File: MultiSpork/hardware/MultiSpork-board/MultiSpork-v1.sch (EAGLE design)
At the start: 215 parts, among them J1 U.FL, Q2 32.768 kHz, Q3 40 MHz, Q4 MMBT3904, Q5 MMBT3904, U1 USD-SOCKETNEW, U10 M25PX80, U2 SAM3SA-MU, U3 MAX11300GTL, U4 LT3580EMS8E, U5 LT3580EMS8E, U6 LT3580EMS8E, U7 MCP73831, U8 LT3580EMS8E, U9 CC3100

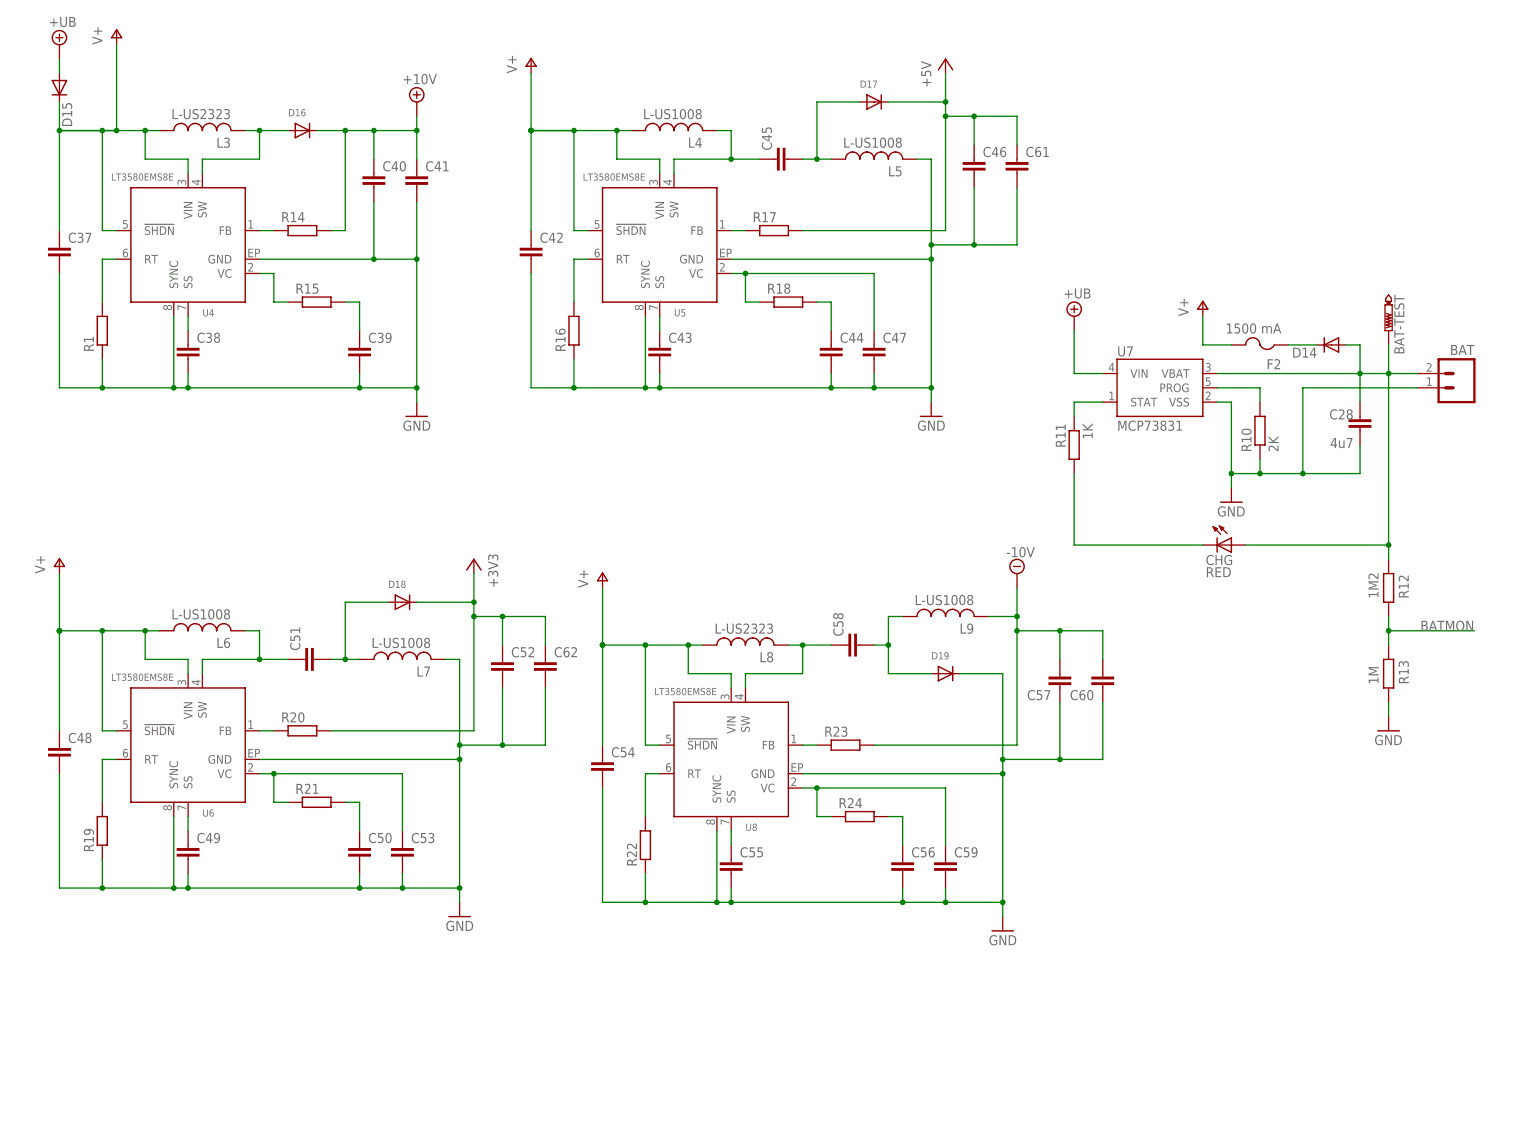
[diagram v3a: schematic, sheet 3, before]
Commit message: -- Updated MAX11300 footprint with rounded pads to account for minimum clearances at the corners -- Added a switch to turn the regulators on and off -- Routed USB -- Routed SPI busses -- Routed analog inputs to protection components
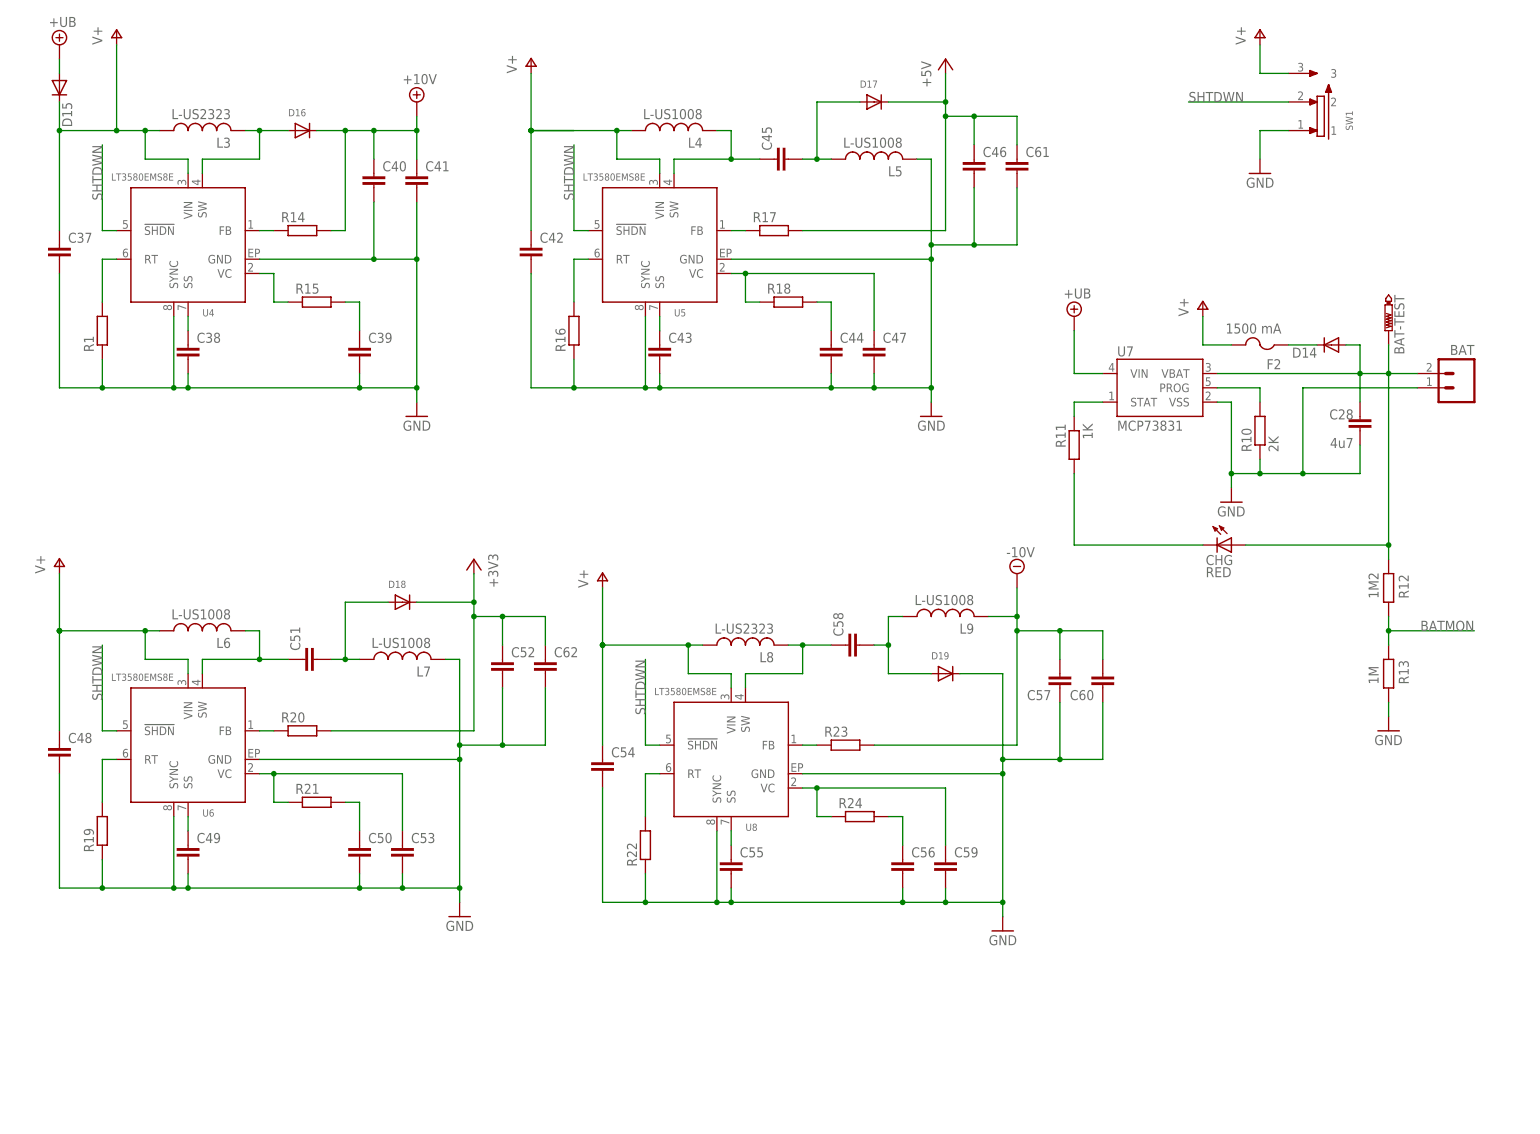
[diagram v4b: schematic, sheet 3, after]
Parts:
- added SW1: JS102011SAQN, logos-switch:JS102011SAQN
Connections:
- new net SHTDWN: SW1.2, U4.!SHDN!, U5.!SHDN!, U6.!SHDN!, U8.!SHDN!
- net GND: now also SW1.1
- net V+: now also SW1.3; no longer U4.!SHDN!, U5.!SHDN!, U6.!SHDN!, U8.!SHDN!
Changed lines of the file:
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@@
 <part name="R40" library="resistor" deviceset="R-EU_" device="R1206"/>
 <part name="J1" library="SparkFun-Connectors" deviceset="U.FL" device="" value="U.FL"/>
+<part name="SW1" library="logos-switch" deviceset="JS102011SAQN" device=""/>
+<part name="P+7" library="supply1" deviceset="V+" device=""/>
+<part name="GND29" library="supply1" deviceset="GND" device=""/>
 </parts>
 <sheets>
@@
 <instance part="C52" gate="G$1" x="93.98" y="88.9"/>
 <instance part="C62" gate="G$1" x="101.6" y="88.9"/>
+<instance part="SW1" gate="G$1" x="238.76" y="187.96" rot="MR90"/>
+<instance part="P+7" gate="1" x="228.6" y="200.66"/>
+<instance part="GND29" gate="1" x="228.6" y="175.26" rot="MR0"/>
 </instances>
 <busses>
@@
 <junction x="193.04" y="71.12"/>
 </segment>
+<segment>
+<pinref part="SW1" gate="G$1" pin="1"/>
+<pinref part="GND29" gate="1" pin="GND"/>
+<wire x1="228.6" y1="177.8" x2="228.6" y2="182.88" width="0.1524" layer="91"/>
+<wire x1="228.6" y1="182.88" x2="233.68" y2="182.88" width="0.1524" layer="91"/>
+</segment>
 </net>
 <net name="+3V3" class="0">
@@
 <segment>
 <pinref part="P+5" gate="1" pin="V+"/>
-<wire x1="15.24" y1="182.88" x2="25.4" y2="182.88" width="0.1524" layer="91"/>
 <wire x1="25.4" y1="182.88" x2="25.4" y2="198.12" width="0.1524" layer="91"/>
 <pinref part="D15" gate="G$1" pin="C"/>
@@
 <wire x1="30.48" y1="182.88" x2="33.02" y2="182.88" width="0.1524" layer="91"/>
 <wire x1="30.48" y1="182.88" x2="25.4" y2="182.88" width="0.1524" layer="91"/>
-<wire x1="25.4" y1="182.88" x2="22.86" y2="182.88" width="0.1524" layer="91"/>
-<wire x1="22.86" y1="182.88" x2="22.86" y2="165.1" width="0.1524" layer="91"/>
-<pinref part="U4" gate="G$1" pin="!SHDN!"/>
-<wire x1="22.86" y1="165.1" x2="25.4" y2="165.1" width="0.1524" layer="91"/>
 <junction x="30.48" y="182.88"/>
 <pinref part="C37" gate="G$1" pin="1"/>
-<wire x1="22.86" y1="182.88" x2="15.24" y2="182.88" width="0.1524" layer="91"/>
+<wire x1="25.4" y1="182.88" x2="15.24" y2="182.88" width="0.1524" layer="91"/>
 <wire x1="15.24" y1="182.88" x2="15.24" y2="165.1" width="0.1524" layer="91"/>
-<junction x="22.86" y="182.88"/>
 <junction x="25.4" y="182.88"/>
 <junction x="15.24" y="182.88"/>
@@
 <wire x1="114.3" y1="182.88" x2="116.84" y2="182.88" width="0.1524" layer="91"/>
 <wire x1="114.3" y1="182.88" x2="99.06" y2="182.88" width="0.1524" layer="91"/>
-<wire x1="106.68" y1="182.88" x2="106.68" y2="165.1" width="0.1524" layer="91"/>
-<pinref part="U5" gate="G$1" pin="!SHDN!"/>
-<wire x1="106.68" y1="165.1" x2="109.22" y2="165.1" width="0.1524" layer="91"/>
 <junction x="114.3" y="182.88"/>
 <pinref part="C42" gate="G$1" pin="1"/>
 <wire x1="106.68" y1="182.88" x2="99.06" y2="182.88" width="0.1524" layer="91"/>
 <wire x1="99.06" y1="182.88" x2="99.06" y2="165.1" width="0.1524" layer="91"/>
-<junction x="106.68" y="182.88"/>
 <junction x="99.06" y="182.88"/>
 <junction x="99.06" y="182.88"/>
@@
 <pinref part="L6" gate="G$1" pin="1"/>
 <wire x1="30.48" y1="93.98" x2="33.02" y2="93.98" width="0.1524" layer="91"/>
-<wire x1="30.48" y1="93.98" x2="22.86" y2="93.98" width="0.1524" layer="91"/>
-<wire x1="22.86" y1="93.98" x2="22.86" y2="76.2" width="0.1524" layer="91"/>
-<pinref part="U6" gate="G$1" pin="!SHDN!"/>
-<wire x1="22.86" y1="76.2" x2="25.4" y2="76.2" width="0.1524" layer="91"/>
 <junction x="30.48" y="93.98"/>
 <pinref part="C48" gate="G$1" pin="1"/>
-<wire x1="22.86" y1="93.98" x2="15.24" y2="93.98" width="0.1524" layer="91"/>
+<wire x1="30.48" y1="93.98" x2="15.24" y2="93.98" width="0.1524" layer="91"/>
 <wire x1="15.24" y1="93.98" x2="15.24" y2="76.2" width="0.1524" layer="91"/>
-<junction x="22.86" y="93.98"/>
 <junction x="15.24" y="93.98"/>
 <junction x="15.24" y="93.98"/>
@@
 <pinref part="L8" gate="G$1" pin="1"/>
 <wire x1="127" y1="91.44" x2="129.54" y2="91.44" width="0.1524" layer="91"/>
-<wire x1="127" y1="91.44" x2="119.38" y2="91.44" width="0.1524" layer="91"/>
-<wire x1="119.38" y1="91.44" x2="119.38" y2="73.66" width="0.1524" layer="91"/>
-<pinref part="U8" gate="G$1" pin="!SHDN!"/>
-<wire x1="119.38" y1="73.66" x2="121.92" y2="73.66" width="0.1524" layer="91"/>
 <junction x="127" y="91.44"/>
 <pinref part="C54" gate="G$1" pin="1"/>
-<wire x1="119.38" y1="91.44" x2="111.76" y2="91.44" width="0.1524" layer="91"/>
+<wire x1="127" y1="91.44" x2="111.76" y2="91.44" width="0.1524" layer="91"/>
 <wire x1="111.76" y1="91.44" x2="111.76" y2="73.66" width="0.1524" layer="91"/>
-<junction x="119.38" y="91.44"/>
 <junction x="111.76" y="91.44"/>
 <junction x="111.76" y="91.44"/>
+</segment>
+<segment>
+<pinref part="SW1" gate="G$1" pin="3"/>
+<pinref part="P+7" gate="1" pin="V+"/>
+<wire x1="228.6" y1="198.12" x2="228.6" y2="193.04" width="0.1524" layer="91"/>
+<wire x1="228.6" y1="193.04" x2="233.68" y2="193.04" width="0.1524" layer="91"/>
 </segment>
 </net>
@@
 </segment>
 </net>
+<net name="SHTDWN" class="0">
+<segment>
+<pinref part="SW1" gate="G$1" pin="2"/>
+<wire x1="233.68" y1="187.96" x2="215.9" y2="187.96" width="0.1524" layer="91"/>
+<label x="215.9" y="187.96" size="1.778" layer="95"/>
+</segment>
+<segment>
+<pinref part="U8" gate="G$1" pin="!SHDN!"/>
+<wire x1="119.38" y1="73.66" x2="121.92" y2="73.66" width="0.1524" layer="91"/>
+<wire x1="119.38" y1="73.66" x2="119.38" y2="88.9" width="0.1524" layer="91"/>
+<label x="119.38" y="88.9" size="1.778" layer="95" rot="MR270"/>
+</segment>
+<segment>
+<pinref part="U6" gate="G$1" pin="!SHDN!"/>
+<wire x1="22.86" y1="76.2" x2="25.4" y2="76.2" width="0.1524" layer="91"/>
+<wire x1="22.86" y1="76.2" x2="22.86" y2="91.44" width="0.1524" layer="91"/>
+<label x="22.86" y="91.44" size="1.778" layer="95" rot="MR270"/>
+</segment>
+<segment>
+<pinref part="U4" gate="G$1" pin="!SHDN!"/>
+<wire x1="22.86" y1="165.1" x2="25.4" y2="165.1" width="0.1524" layer="91"/>
+<wire x1="22.86" y1="165.1" x2="22.86" y2="180.34" width="0.1524" layer="91"/>
+<label x="22.86" y="180.34" size="1.778" layer="95" rot="MR270"/>
+</segment>
+<segment>
+<pinref part="U5" gate="G$1" pin="!SHDN!"/>
+<wire x1="106.68" y1="165.1" x2="109.22" y2="165.1" width="0.1524" layer="91"/>
+<wire x1="106.68" y1="165.1" x2="106.68" y2="180.34" width="0.1524" layer="91"/>
+<label x="106.68" y="180.34" size="1.778" layer="95" rot="MR270"/>
+</segment>
+</net>

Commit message: Finished routing
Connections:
- net N$115 renamed D1P
- net N$116 renamed D1N
- net N$117 renamed D0N
- net N$118 renamed D0P
- net N$19 renamed PLL-GND
- net N$32 renamed ADC_REF
- net N$33 renamed DAC_REF
- net N$34 renamed PORT00'
- net N$35 renamed PORT01'
- net N$36 renamed PORT02'
- net N$37 renamed PORT03'
- net N$38 renamed PORT04'
- net N$39 renamed PORT05'
- net N$40 renamed PORT06'
- net N$41 renamed PORT07'
- net N$42 renamed PORT08'
- net N$43 renamed PORT09'
- net N$44 renamed PORT10'
- net N$45 renamed PORT11'
- net N$46 renamed PORT12'
- net N$47 renamed PORT13'
- net N$49 renamed PORT14'
- net N$50 renamed PORT15'
- net N$51 renamed PORT16'
- net N$52 renamed PORT17'
- net N$53 renamed PORT18'
- net N$54 renamed PORT19'
- net N$56 renamed VDD_IO
- net N$79 renamed VIN_IO2
- net N$80 renamed VIN_DIG
- net N$81 renamed VIN_ANA
- net N$83 renamed VIN_PA
- net N$84 renamed ANA_SW
- net N$85 renamed VDD_PA
- net N$87 renamed PA_SWP
- net N$88 renamed PA_SWN
- net N$90 renamed VDD_DIG
- net N$92 renamed VDD_RAM
- net N$93 renamed VDD_PLL
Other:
- moved on the sheet: C24, L12, U3-REF

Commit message: .\s5uqt2as.xa0.txt
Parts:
- ACC, JP2, JP3: PARTNO (none) -> *
- ANALOG: PARTNO (none) -> 76385-316LF
- C1, C2, C3, C4, C5: PARTNO (none) -> VJ0603A330JXACW1BC
- C10, C12, C13, C14, C15, C19, C20, C22, C25, C26, C29, C31, C33, C63, C67, C69, C70, C71, C73, C74, C75, C76, C77, C80, C85, C9: PARTNO (none) -> CC0603KRX7R9BB104
- C11, C30, C32, C34: PARTNO (none) -> UMK107BJ105KA-T
- C16, C17, C21, C24, C27, C64, C65, C66: PARTNO (none) -> GRM188F51A475ZE20D
- C18, C68, C72: PARTNO (none) -> EMK107BBJ106MA-T
- C23: PARTNO (none) -> C1608X7R1A225K
- C35, C36, C81, C82: value (none) -> 33p; PARTNO (none) -> VJ0603A330JXACW1BC
- C37, C42, C48, C54: value (none) -> 4u7; PARTNO (none) -> TMK325B7475KN-T
- C38, C43, C49, C55: value (none) -> 100n; PARTNO (none) -> CC0603KRX7R9BB104
- C39, C56: value (none) -> 2n2; PARTNO (none) -> VJ0603Y222KXACW1BC
- C40, C41, C46, C52, C57, C60, C61, C62: value (none) -> 10u; PARTNO (none) -> UMK325BJ106MM
- C44, C50: value (none) -> 1n; PARTNO (none) -> UMK107SD102KA-T
- C45, C51, C58: value (none) -> 1u; PARTNO (none) -> TMK325B7105KD-T
- C47, C53: value (none) -> 22p; PARTNO (none) -> GQM1885C1H220JB01D
- C59: value (none) -> DNP; DNP (none) -> T; PARTNO (none) -> DNP
- C6: PARTNO (none) -> CL10B103KB8NCNC
- C7, C8: PARTNO (none) -> C3216X5R1E106M
- C78, C79: PARTNO (none) -> GRM31CR61C226ME15L
- C83, C84: value (none) -> 15p; PARTNO (none) -> VJ0603A150JXACW1BC
- C86, C87: PARTNO (none) -> TAJC107K016RNJ
- D1, D10, D11, D12, D13, D2, D3, D4, D5, D6, D7, D8, D9: PARTNO (none) -> SD103ASDM-7
- D16, D18, D19: value (none) -> 2A/40V; PARTNO LSM115JE3 -> CD214A-B240LLF
- D17: PARTNO LSM115JE3 -> PMEG3020ER,115
- ERASE, JTAGSEL, JTAG_RST, TST: BOM (none) -> EXCLUDE
- F1: PARTNO (none) -> 1206L050/15YR
- F10, F11, F12, F13, F14, F15, F16, F17, F18, F19, F20, F21, F22, F3, F4, F5, F6, F7, F8, F9: PARTNO (none) -> femtoSMDC008F-02
- F2: value 1500 mA -> 1000 mA; PARTNO (none) -> 0ZCJ0100FF2E
- FL1: PARTNO (none) -> DEA202450BT-7210A1
- H1, H2, H3, H4: BOM (none) -> EXCLUDE; PARTNO (none) -> *
- J1: PARTNO (none) -> U.FL-R-SMT(10)
- JP1: PARTNO (none) -> M50-3500542
- L1: PARTNO (none) -> MI0805K400R-10
- L10, L12: PARTNO (none) -> LQM31PN2R2M00L
- L11: PARTNO (none) -> LQM31PN1R0MC0L
- L2: PARTNO (none) -> LQH31CN100K03L
- L3: value L-US2323 -> 3u9; PARTNO (none) -> SRR5018-3R9Y
- L4, L5, L6, L7: value L-US1008 -> 2u2; PARTNO (none) -> 252012CDMCDS-2R2MC
- L8: value L-US2323 -> 5u3; PARTNO (none) -> SRR5028-5R3Y
- L9: value L-US1008 -> 5u6; PARTNO (none) -> 1008 (2520 metric)
- Q1: value (none) -> 20 MHz; PARTNO (none) -> ECS-200-20-3X-TR
- Q2: PARTNO (none) -> ECS-.327-7-34B-TR
- Q3: PARTNO (none) -> ECS-400-20-3X-EN-TR
- Q4, Q5: PARTNO (none) -> MMBT3904
- R1, R16, R19, R22: value (none) -> 47K; PARTNO (none) -> MCT06030C4702FP500
- R14: value (none) -> 105K; PARTNO (none) -> CRCW0603105KFKEA
- R15, R18, R21, R24, R36: value (none) -> 10K; PARTNO (none) -> RNCP0603FTD10K0
- R17: value (none) -> 45K3; PARTNO (none) -> CRCW060345K3FKEA
- R2, R6, R7: PARTNO (none) -> 742C083101JPTR
- R20: value (none) -> 24K; PARTNO (none) -> CRCW060324K0FKEA
- R23: value (none) -> 120K; PARTNO (none) -> AF0603FR-07120KL
- R25, R32, R9: PARTNO (none) -> RNCP0603FTD10K0
- R26, R27, R28, R31, R33, R34, R35, R37, R38, R39: PARTNO (none) -> CRCW0603100KFKEA
- R29, R30: PARTNO (none) -> RC1608J472CS
- R3, R4: PARTNO (none) -> CRCW060327R0FKEA
- R40: value (none) -> 1R; PARTNO (none) -> CRCW12061R00FKEA
- R5: PARTNO (none) -> ERJ-3GEYJ152V
- R8: PARTNO (none) -> ERJ-3GEYJ1R0V
- RESET: PARTNO (none) -> SKHMQKE010
- SW1: PARTNO (none) -> JS102011SAQN
- U1: PARTNO (none) -> 502570-0893
- U10: PARTNO (none) -> M25PX80-VMN6TP
- U2: PARTNO (none) -> ATSAM3S4AA-MU
- U3: PARTNO (none) -> MAX11300GTL+
- U4, U5, U6, U8: PARTNO (none) -> LT3580EMS8E#PBF
- U9: PARTNO (none) -> CC3100
- USB-IN: PARTNO (none) -> 20236
